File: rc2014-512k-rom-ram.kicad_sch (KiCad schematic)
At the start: 15 parts, among them J1 RC2014_Bus, U1 SST39SF040, U2 AS6C4008-55PCN, U3 74LS139, U4 74LS74, U5 74LS670, U6 74LS670, U7 74LS138

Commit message: Finally fully routed
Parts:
- removed C6: 0.1µF, Capacitor_THT:C_Disc_D4.7mm_W2.5mm_P5.00mm, symbol Device:C_Small
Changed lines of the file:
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@@
   (junction (at 114.3 175.895) (diameter 0) (color 0 0 0 0)
   )
-  (junction (at 257.81 25.4) (diameter 0) (color 0 0 0 0)
-  )
   (junction (at 223.52 25.4) (diameter 0) (color 0 0 0 0)
   )
@@
   )
   (junction (at 114.3 166.37) (diameter 0) (color 0 0 0 0)
-  )
-  (junction (at 257.81 30.48) (diameter 0) (color 0 0 0 0)
   )
   (junction (at 246.38 30.48) (diameter 0) (color 0 0 0 0)
@@
     (stroke (width 0) (type default))
   )
-  (wire (pts (xy 257.81 25.4) (xy 269.875 25.4))
-    (stroke (width 0) (type default))
-  )
   (wire (pts (xy 118.745 142.24) (xy 111.125 142.24))
     (stroke (width 0) (type default))
@@
   )
   (wire (pts (xy 206.375 24.765) (xy 206.375 25.4))
-    (stroke (width 0) (type default))
-  )
-  (wire (pts (xy 269.875 30.48) (xy 257.81 30.48))
     (stroke (width 0) (type default))
   )
@@
         )
       )
-    )
-  )
-  (symbol (lib_id "Device:C_Small") (at 269.875 27.94 0) (unit 1)
-    (in_bom yes) (on_board yes) (dnp no) (fields_autoplaced)
-    (property "Reference" "C6" (at 273.05 26.6763 0)
-      (effects (font (size 1.27 1.27)) (justify left))
-    )
-    (property "Value" "0.1µF" (at 273.05 29.2163 0)
-      (effects (font (size 1.27 1.27)) (justify left))
-    )
-    (property "Footprint" "Capacitor_THT:C_Disc_D4.7mm_W2.5mm_P5.00mm" (at 269.875 27.94 0)
-      (effects (font (size 1.27 1.27)) hide)
-    )
-    (property "Datasheet" "~" (at 269.875 27.94 0)
-      (effects (font (size 1.27 1.27)) hide)
-    )
-    (pin "2")
-    (pin "1")
-    (instances
-      (project "rc2014-512k-rom-ram"
-        (path "/99fcc25a-a002-421a-a96f-92f3cfdfc8b8"
-          (reference "C6") (unit 1)
-        )
-      )

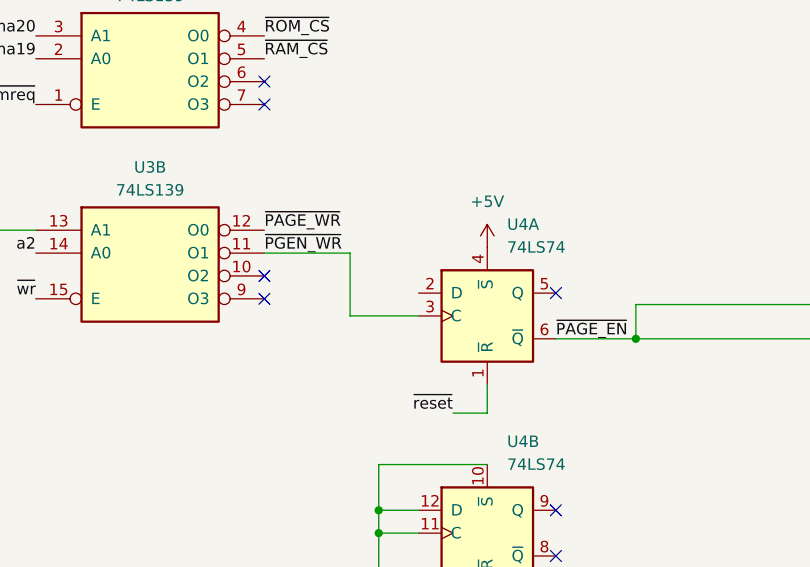
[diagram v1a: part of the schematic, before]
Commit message: Fix missing d0 line
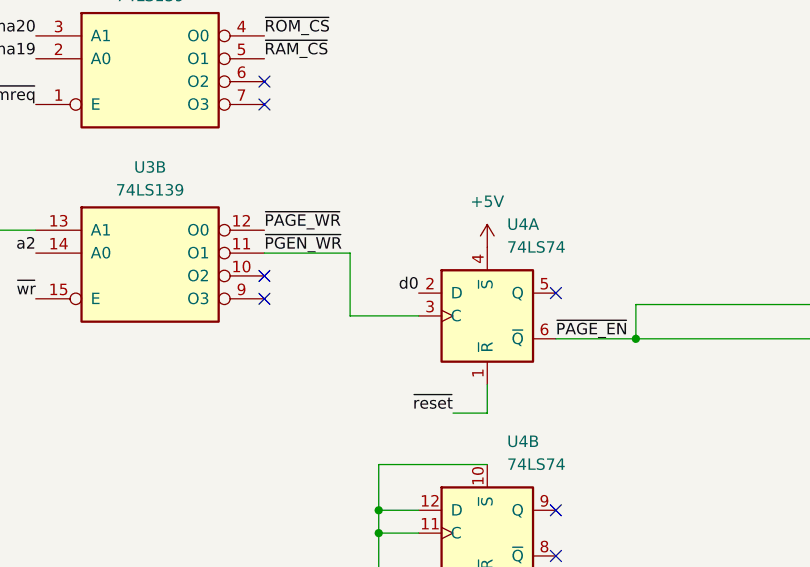
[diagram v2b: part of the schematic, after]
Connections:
- net d0: now also U4.2 (D)

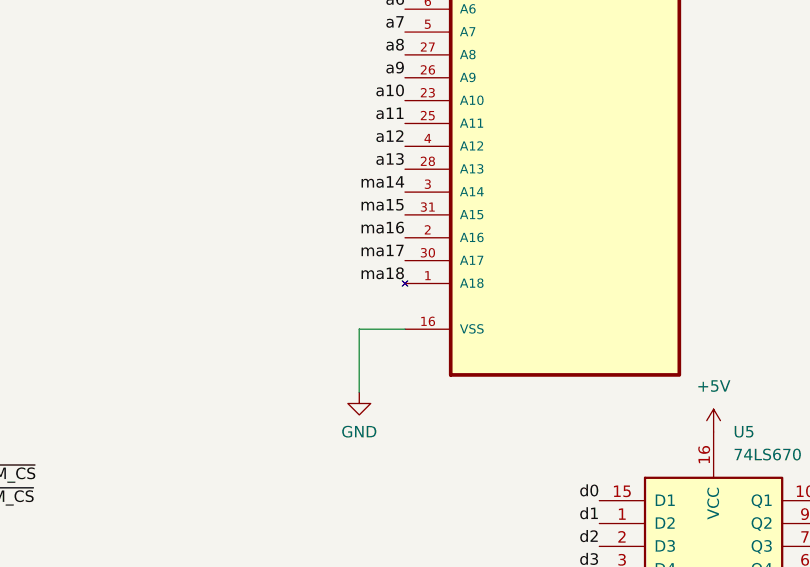
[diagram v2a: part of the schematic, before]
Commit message: A18 shouldn't be broken on 4008
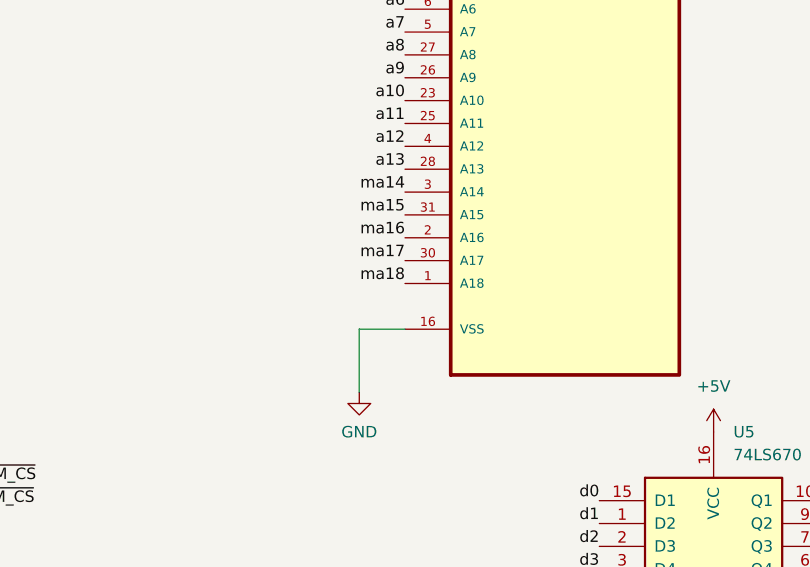
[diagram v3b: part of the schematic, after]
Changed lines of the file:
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@@
 			)
 		)
-		(property "Description" "\nAS6C4008 Series 4-Mbit (512 K x 8) 3 V 55 ns CMOS Static RAM - PDIP-32\n"
+		(property "Description" "AS6C4008 Series 4-Mbit (512 K x 8) 3 V 55 ns CMOS Static RAM - PDIP-32"
 			(at 167.64 58.42 0)
 			(effects

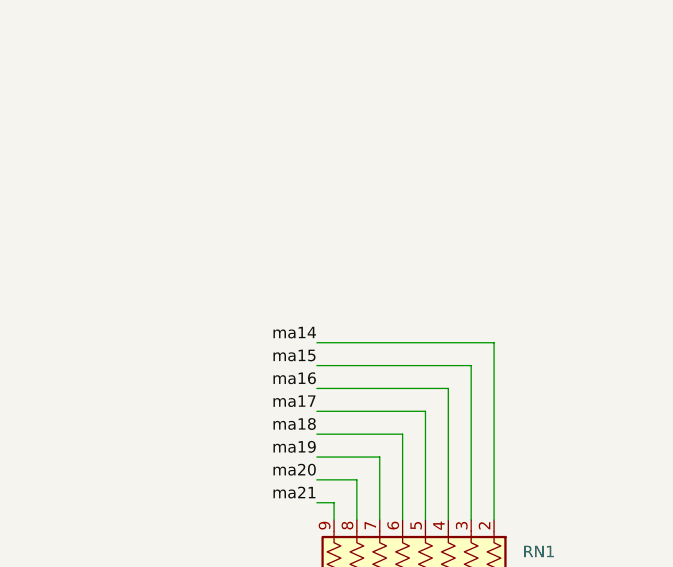
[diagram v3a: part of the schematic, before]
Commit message: Fix root symbol
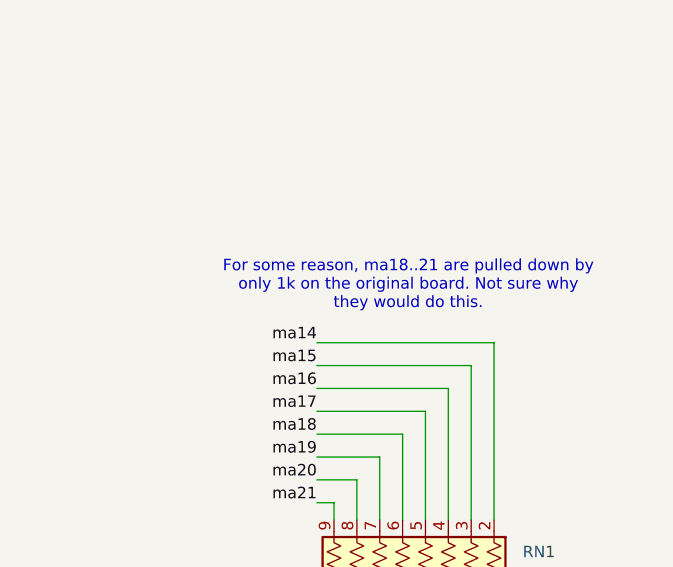
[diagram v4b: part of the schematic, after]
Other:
- note added: "For some reason, ma18..21 are pulled down by only 1k on the original board. Not sure why they would do this."
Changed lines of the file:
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@@
+		)
+	)
+	(text "For some reason, ma18..21 are pulled down by\nonly 1k on the original board. Not sure why\nthey would do this."
+		(exclude_from_sim no)
+		(at 259.08 63.5 0)
+		(effects
+			(font
+				(size 1.27 1.27)
+			)
 		)
 	)

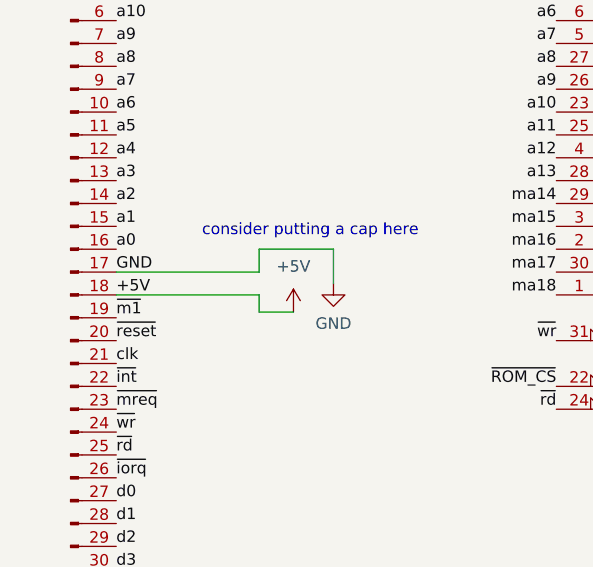
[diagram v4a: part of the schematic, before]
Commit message: Fix power flag complaint
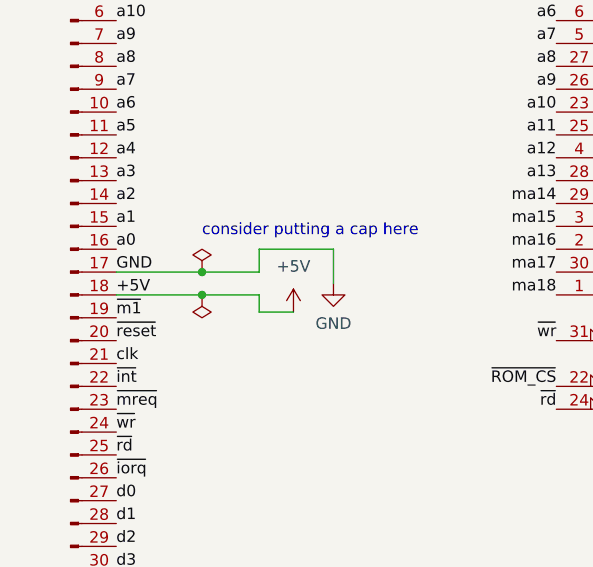
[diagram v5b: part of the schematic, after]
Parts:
- U2: footprint Package_DIP:DIP-32_W15.24mm_Socket_LongPads -> AS6C4008-55PCN:DIP254P1524X393-32; Description_1 (none) -> AS6C4008 Series 4-Mbit (512 K x 8) 3 V 55 ns CMOS Static RA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
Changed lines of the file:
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@@
 	)
 	(junction
+		(at 33.02 67.945)
+		(diameter 0)
+		(color 0 0 0 0)
+	)
+	(junction
 		(at 114.3 175.895)
 		(diameter 0)
@@
 	)
 	(junction
+		(at 33.02 70.485)
+		(diameter 0)
+		(color 0 0 0 0)
+	)
+	(junction
 		(at 114.3 166.37)
 		(diameter 0)
@@
 	(wire
 		(pts
-			(xy 39.37 67.945) (xy 23.495 67.945)
+			(xy 39.37 67.945) (xy 33.02 67.945)
 		)
 		(stroke
@@
 	(wire
 		(pts
-			(xy 23.495 70.485) (xy 39.37 70.485)
+			(xy 23.495 70.485) (xy 33.02 70.485)
 		)
 		(stroke
@@
 	(wire
 		(pts
+			(xy 33.02 67.945) (xy 23.495 67.945)
+		)
+		(stroke
+			(width 0)
+			(type default)
+		)
+	)
+	(wire
+		(pts
 			(xy 248.92 82.55) (xy 255.905 82.55)
 		)
@@
 	(wire
 		(pts
+			(xy 33.02 70.485) (xy 39.37 70.485)
+		)
+		(stroke
+			(width 0)
+			(type default)
+		)
+	)
+	(wire
+		(pts
 			(xy 47.625 65.405) (xy 47.625 69.215)
 		)
@@
 	)
 	(symbol
+		(lib_id "power:PWR_FLAG")
+		(at 33.02 70.485 180)
+		(unit 1)
+		(exclude_from_sim no)
+		(in_bom yes)
+		(on_board yes)
+		(dnp no)
+		(fields_autoplaced yes)
+		(property "Reference" "#FLG02"
+			(at 33.02 72.39 0)
+			(effects
+				(font
+					(size 1.27 1.27)
+				)
+				(hide yes)
+			)
+		)
+		(property "Value" "PWR_FLAG"
+			(at 33.02 74.93 0)
+			(effects
+				(font
+					(size 1.27 1.27)
+				)
+				(hide yes)
+			)
+		)
+		(property "Footprint" ""
+			(at 33.02 70.485 0)
+			(effects
+				(font
+					(size 1.27 1.27)
+				)
+				(hide yes)
+			)
+		)
+		(property "Datasheet" "~"
+			(at 33.02 70.485 0)
+			(effects
+				(font
+					(size 1.27 1.27)
+				)
+				(hide yes)
+			)
+		)
+		(property "Description" "Special symbol for telling ERC where power comes from"
+			(at 33.02 70.485 0)
+			(effects
+				(font
+					(size 1.27 1.27)
+				)
+				(hide yes)
+			)
+		)
+		(pin "1"
+		)
+		(instances
+			(project "rc2014-512k-rom-ram"
+				(path "/99fcc25a-a002-421a-a96f-92f3cfdfc8b8"
+					(reference "#FLG02")
+					(unit 1)
+				)
+			)
+		)
+	)
+	(symbol
 		(lib_id "power:+5V")
 		(at 57.15 150.495 0)
@@
 			)
 		)
-		(property "Footprint" "Package_DIP:DIP-32_W15.24mm_Socket_LongPads"
+		(property "Footprint" "AS6C4008-55PCN:DIP254P1524X393-32"
 			(at 167.64 58.42 0)
 			(effects
@@
 			)
 		)
+		(property "Description_1" "\nAS6C4008 Series 4-Mbit (512 K x 8) 3 V 55 ns CMOS Static RAM - PDIP-32\n"
+			(at 167.64 58.42 0)
+			(effects
+				(font
+					(size 1.27 1.27)
+				)
+				(justify bottom)
+				(hide yes)
+			)
+		)
 		(pin "3"
 		)
@@
 					(unit 1)
 				)
+			)
+		)
+	)
+	(symbol
+		(lib_id "power:PWR_FLAG")
+		(at 33.02 67.945 0)
+		(unit 1)
+		(exclude_from_sim no)
+		(in_bom yes)
+		(on_board yes)
+		(dnp no)
+		(fields_autoplaced yes)
+		(property "Reference" "#FLG01"
+			(at 33.02 66.04 0)
+			(effects
+				(font
+					(size 1.27 1.27)
+				)
+				(hide yes)
+			)
+		)
+		(property "Value" "PWR_FLAG"
+			(at 33.02 63.5 0)
+			(effects
+				(font
+					(size 1.27 1.27)
+				)
+				(hide yes)
+			)
+		)
+		(property "Footprint" ""
+			(at 33.02 67.945 0)
+			(effects
+				(font
+					(size 1.27 1.27)
+				)
+				(hide yes)
+			)
+		)
+		(property "Datasheet" "~"
+			(at 33.02 67.945 0)
+			(effects
+				(font
+					(size 1.27 1.27)
+				)
+				(hide yes)
+			)
+		)
+		(property "Description" "Special symbol for telling ERC where power comes from"
+			(at 33.02 67.945 0)
+			(effects
+				(font
+					(size 1.27 1.27)
+				)
+				(hide yes)
+			)
+		)
+		(pin "1"
+		)
+		(instances
+			(project ""
+				(path "/99fcc25a-a002-421a-a96f-92f3cfdfc8b8"
+					(reference "#FLG01")
+					(unit 1)
+				)
